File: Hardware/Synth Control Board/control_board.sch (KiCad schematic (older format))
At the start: 48 parts, among them J1 Conn_01x13, J10 Conn_01x05, J11 Conn_01x08, J2 Conn_01x03, J3 Conn_01x13, J4 Conn_01x13, J5 Conn_01x08, J6 Conn_01x13, J7 Conn_01x05, J8 Conn_01x05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

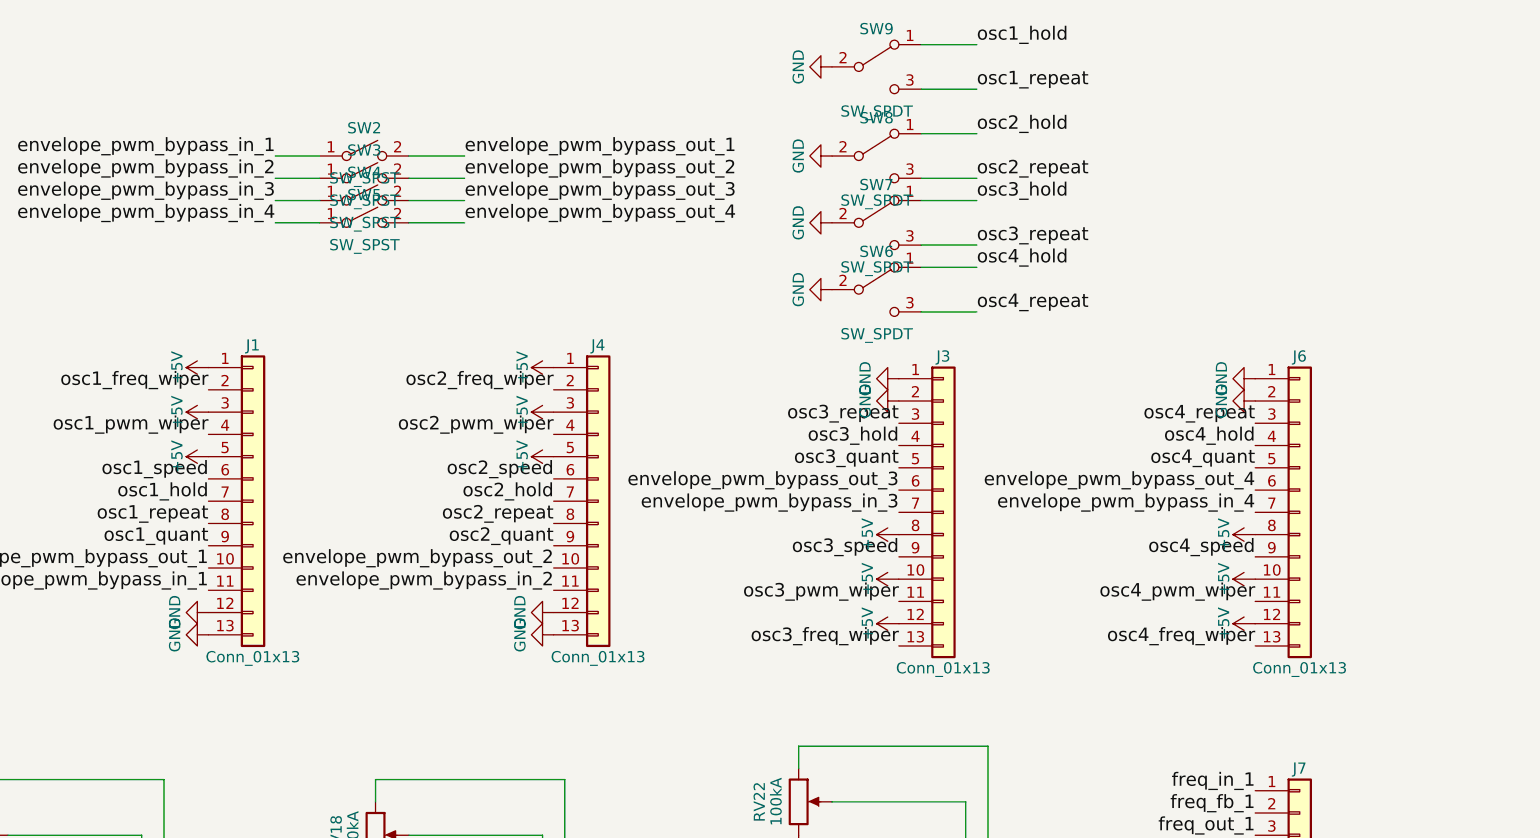
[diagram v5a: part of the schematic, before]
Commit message: add quantization again, fix connectors again, add mounting holes to main board
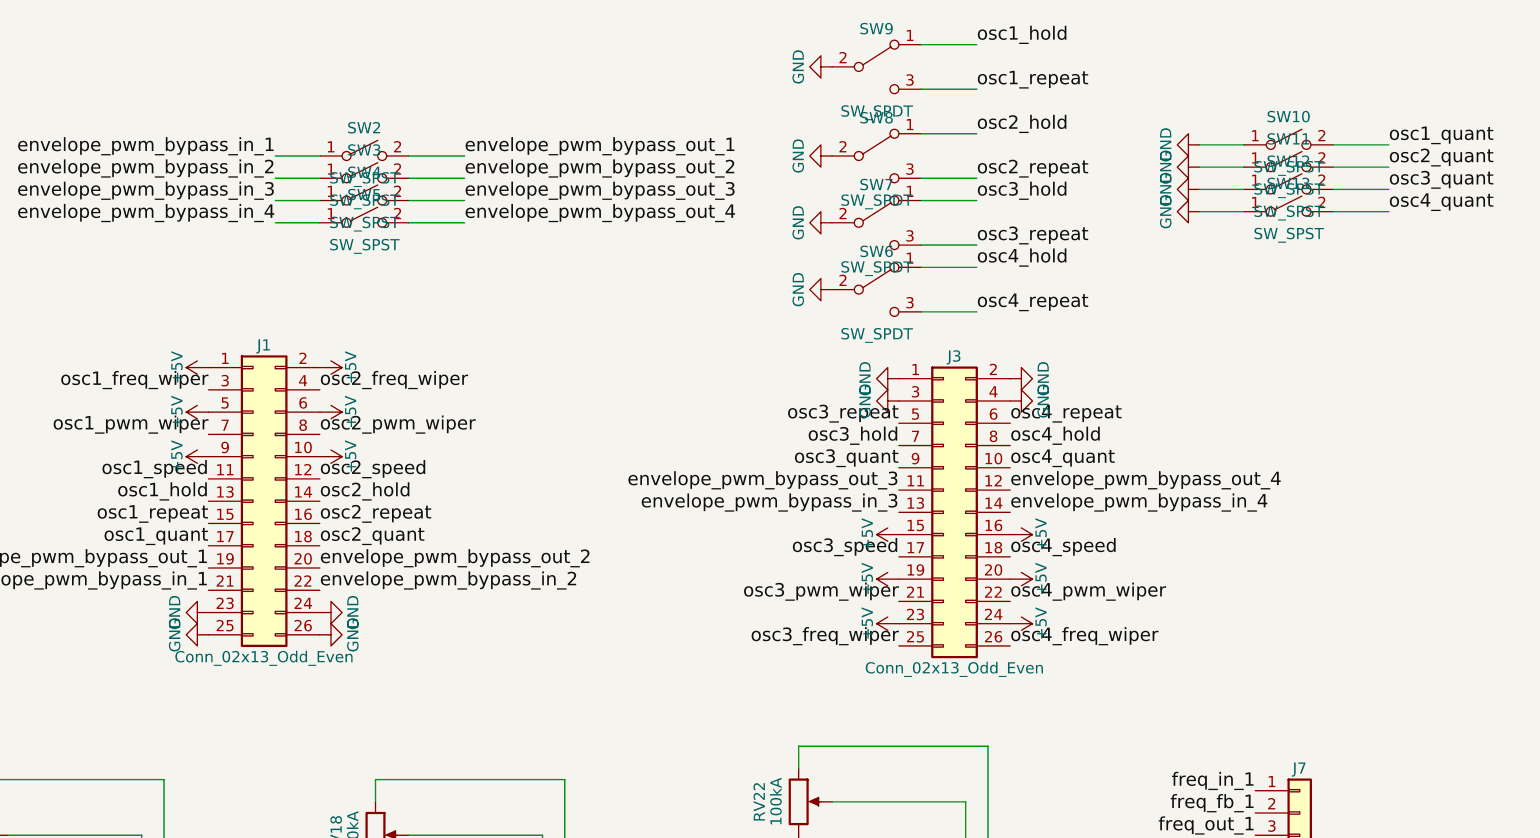
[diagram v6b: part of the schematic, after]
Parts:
- removed J1, J3, J4, J6: Conn_01x13, Pin_Headers:Pin_Header_Straight_1x13_Pitch2.54mm, symbol Conn_01x13
- added J1, J3: Conn_02x13_Odd_Even, Pin_Headers:Pin_Header_Straight_2x13_Pitch2.54mm, symbol Conn_02x13_Odd_Even
- added SW10, SW11, SW12, SW13: SW_SPST, SparkFun-Electromechanical:SWITCH-SPDT, symbol SW_SPST
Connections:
- net +5V: now also J1.1 (Pin_1), J1.10 (Pin_10), J1.2 (Pin_2), J1.5 (Pin_5), J1.6 (Pin_6), J1.9 (Pin_9), J3.15 (Pin_15), J3.16 (Pin_16), J3.19 (Pin_19), J3.20 (Pin_20), J3.23 (Pin_23), J3.24 (Pin_24)
- net GND: now also J1.23 (Pin_23), J1.24 (Pin_24), J1.25 (Pin_25), J1.26 (Pin_26), J3.1 (Pin_1), J3.2 (Pin_2), J3.3 (Pin_3), J3.4 (Pin_4), SW10.1 (A), SW11.1 (A), SW12.1 (A), SW13.1 (A)
- net envelope_pwm_bypass_in_1: now also J1.21 (Pin_21)
- net envelope_pwm_bypass_in_2: now also J1.22 (Pin_22)
- net envelope_pwm_bypass_in_3: now also J3.13 (Pin_13)
- net envelope_pwm_bypass_in_4: now also J3.14 (Pin_14)
- net envelope_pwm_bypass_out_1: now also J1.19 (Pin_19)
- net envelope_pwm_bypass_out_2: now also J1.20 (Pin_20)
- net envelope_pwm_bypass_out_3: now also J3.11 (Pin_11)
- net envelope_pwm_bypass_out_4: now also J3.12 (Pin_12)
- net osc1_freq_wiper: now also J1.3 (Pin_3)
- net osc1_hold: now also J1.13 (Pin_13)
- net osc1_pwm_wiper: now also J1.7 (Pin_7)
- net osc1_quant: now also J1.17 (Pin_17), SW10.2 (B)
- net osc1_repeat: now also J1.15 (Pin_15)
- net osc1_speed: now also J1.11 (Pin_11)
- net osc2_freq_wiper: now also J1.4 (Pin_4)
- net osc2_hold: now also J1.14 (Pin_14)
- net osc2_pwm_wiper: now also J1.8 (Pin_8)
- net osc2_quant: now also J1.18 (Pin_18), SW11.2 (B)
- net osc2_repeat: now also J1.16 (Pin_16)
- net osc2_speed: now also J1.12 (Pin_12)
- net osc3_freq_wiper: now also J3.25 (Pin_25)
- net osc3_hold: now also J3.7 (Pin_7)
- net osc3_pwm_wiper: now also J3.21 (Pin_21)
- net osc3_quant: now also J3.9 (Pin_9), SW12.2 (B)
- net osc3_repeat: now also J3.5 (Pin_5)
- net osc3_speed: now also J3.17 (Pin_17)
- net osc4_freq_wiper: now also J3.26 (Pin_26)
- net osc4_hold: now also J3.8 (Pin_8)
- net osc4_pwm_wiper: now also J3.22 (Pin_22)
- net osc4_quant: now also J3.10 (Pin_10), SW13.2 (B)
- net osc4_repeat: now also J3.6 (Pin_6)
- net osc4_speed: now also J3.18 (Pin_18)

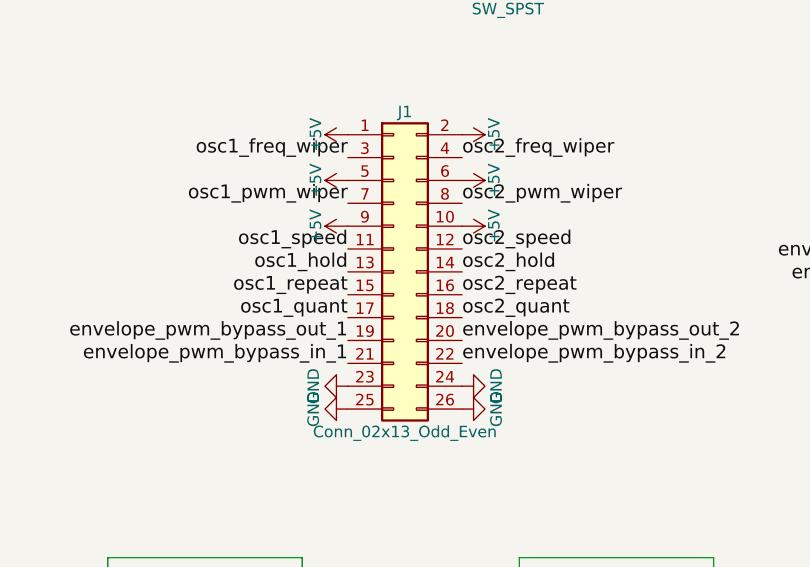
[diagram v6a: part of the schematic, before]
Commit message: reroute first connector on main board
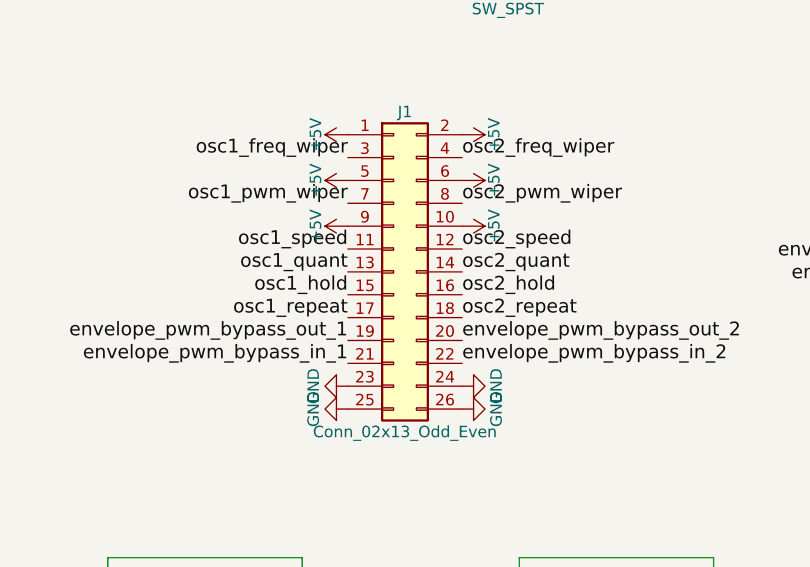
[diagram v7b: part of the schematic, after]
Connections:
- net osc1_hold: now also J1.15 (Pin_15); no longer J1.13 (Pin_13)
- net osc1_quant: now also J1.13 (Pin_13); no longer J1.17 (Pin_17)
- net osc1_repeat: now also J1.17 (Pin_17); no longer J1.15 (Pin_15)
- net osc2_hold: now also J1.16 (Pin_16); no longer J1.14 (Pin_14)
- net osc2_quant: now also J1.14 (Pin_14); no longer J1.18 (Pin_18)
- net osc2_repeat: now also J1.18 (Pin_18); no longer J1.16 (Pin_16)
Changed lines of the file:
@@
 Text Label 5700 2850 2    60   ~ 0
 envelope_pwm_bypass_out_1
-Text Label 5700 2650 2    60   ~ 0
+Text Label 5700 2750 2    60   ~ 0
 osc1_repeat
-Text Label 5700 2750 2    60   ~ 0
+Text Label 5700 2550 2    60   ~ 0
 osc1_quant
 Text Label 2650 5550 2    60   ~ 0
@@
 	0    -1   -1   0
 $EndComp
-Text Label 5700 2550 2    60   ~ 0
+Text Label 5700 2650 2    60   ~ 0
 osc1_hold
 Wire Wire Line
@@
 Text Label 6200 2850 0    60   ~ 0
 envelope_pwm_bypass_out_2
-Text Label 6200 2650 0    60   ~ 0
+Text Label 6200 2750 0    60   ~ 0
 osc2_repeat
-Text Label 6200 2750 0    60   ~ 0
+Text Label 6200 2550 0    60   ~ 0
 osc2_quant
 Text Label 10400 4500 2    60   ~ 0
@@
 	0    1    -1   0
 $EndComp
-Text Label 6200 2550 0    60   ~ 0
+Text Label 6200 2650 0    60   ~ 0
 osc2_hold
 Wire Wire Line

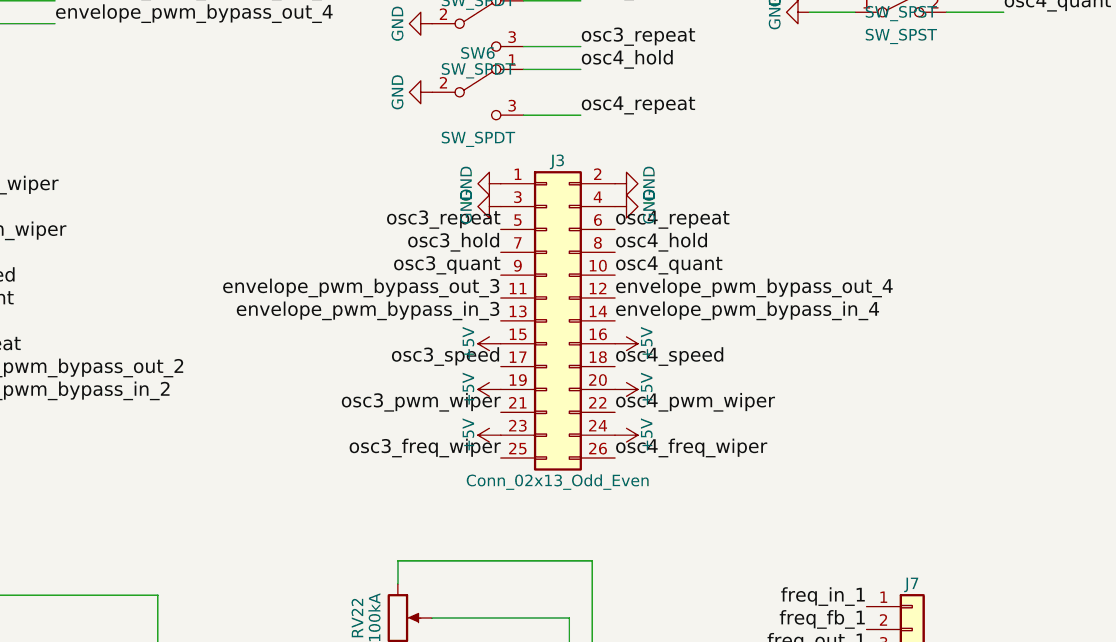
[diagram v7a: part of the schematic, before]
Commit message: reroute connector board with 2-row connectors. Hold switch placement is temporary. Need to find room for this.
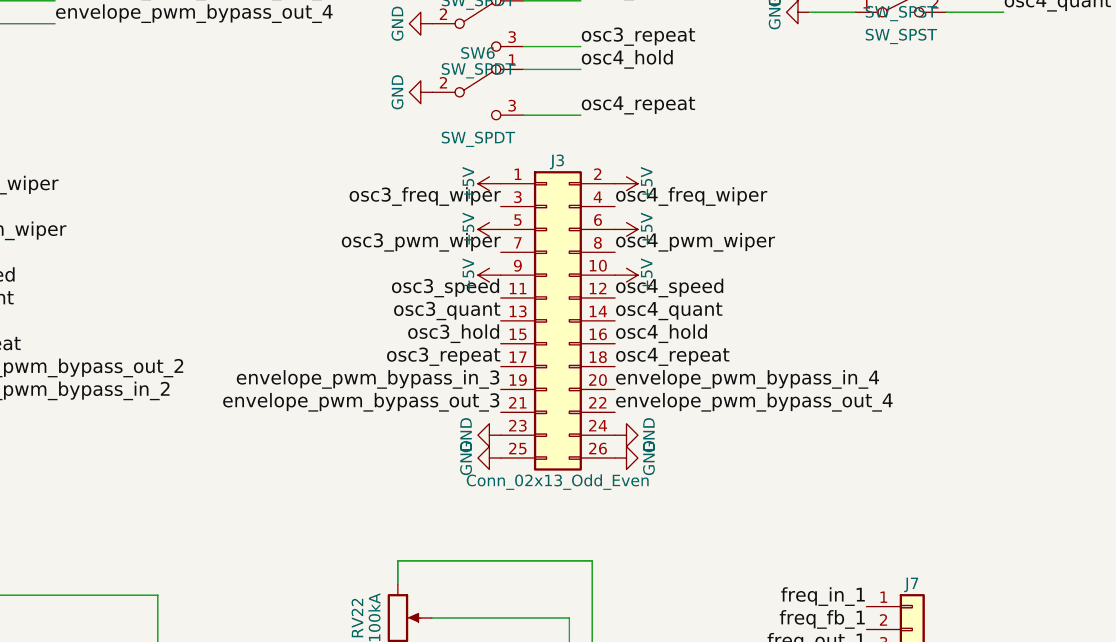
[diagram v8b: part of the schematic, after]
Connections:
- net +5V: now also J3.1 (Pin_1), J3.10 (Pin_10), J3.2 (Pin_2), J3.5 (Pin_5), J3.6 (Pin_6), J3.9 (Pin_9); no longer J3.15 (Pin_15), J3.16 (Pin_16), J3.19 (Pin_19), J3.20 (Pin_20), J3.23 (Pin_23), J3.24 (Pin_24)
- net GND: now also J3.23 (Pin_23), J3.24 (Pin_24), J3.25 (Pin_25), J3.26 (Pin_26); no longer J3.1 (Pin_1), J3.2 (Pin_2), J3.3 (Pin_3), J3.4 (Pin_4)
- net envelope_pwm_bypass_in_3: now also J3.19 (Pin_19); no longer J3.13 (Pin_13)
- net envelope_pwm_bypass_in_4: now also J3.20 (Pin_20); no longer J3.14 (Pin_14)
- net envelope_pwm_bypass_out_3: now also J3.21 (Pin_21); no longer J3.11 (Pin_11)
- net envelope_pwm_bypass_out_4: now also J3.22 (Pin_22); no longer J3.12 (Pin_12)
- net osc3_freq_wiper: now also J3.3 (Pin_3); no longer J3.25 (Pin_25)
- net osc3_hold: now also J3.15 (Pin_15); no longer J3.7 (Pin_7)
- net osc3_pwm_wiper: now also J3.7 (Pin_7); no longer J3.21 (Pin_21)
- net osc3_quant: now also J3.13 (Pin_13); no longer J3.9 (Pin_9)
- net osc3_repeat: now also J3.17 (Pin_17); no longer J3.5 (Pin_5)
- net osc3_speed: now also J3.11 (Pin_11); no longer J3.17 (Pin_17)
- net osc4_freq_wiper: now also J3.4 (Pin_4); no longer J3.26 (Pin_26)
- net osc4_hold: now also J3.16 (Pin_16); no longer J3.8 (Pin_8)
- net osc4_pwm_wiper: now also J3.8 (Pin_8); no longer J3.22 (Pin_22)
- net osc4_quant: now also J3.14 (Pin_14); no longer J3.10 (Pin_10)
- net osc4_repeat: now also J3.18 (Pin_18); no longer J3.6 (Pin_6)
- net osc4_speed: now also J3.12 (Pin_12); no longer J3.18 (Pin_18)
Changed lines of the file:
@@
 Wire Wire Line
 	6200 3150 6200 3150
-Text Label 8800 3200 2    60   ~ 0
+Text Label 8800 2100 2    60   ~ 0
 osc3_freq_wiper
+Text Label 8800 2300 2    60   ~ 0
+osc3_pwm_wiper
+Text Label 8800 2500 2    60   ~ 0
+osc3_speed
+Text Label 8800 2900 2    60   ~ 0
+envelope_pwm_bypass_in_3
 Text Label 8800 3000 2    60   ~ 0
-osc3_pwm_wiper
+envelope_pwm_bypass_out_3
 Text Label 8800 2800 2    60   ~ 0
-osc3_speed
+osc3_repeat
 Text Label 8800 2600 2    60   ~ 0
-envelope_pwm_bypass_in_3
-Text Label 8800 2500 2    60   ~ 0
-envelope_pwm_bypass_out_3
-Text Label 8800 2200 2    60   ~ 0
-osc3_repeat
-Text Label 8800 2400 2    60   ~ 0
 osc3_quant
 Text Label 10400 5200 2    60   ~ 0
@@
 L +5V #PWR037
 U 1 1 5C6257DA
-P 8800 3100
-F 0 "#PWR037" H 8800 2950 50  0001 C CNN
-F 1 "+5V" H 8800 3240 50  0000 C CNN
-F 2 "" H 8800 3100 50  0001 C CNN
-F 3 "" H 8800 3100 50  0001 C CNN
-	1    8800 3100
-	0    -1   -1   0
-$EndComp
-$Comp
-L GND #PWR038
-U 1 1 5C6257E0
 P 8800 2000
-F 0 "#PWR038" H 8800 1750 50  0001 C CNN
-F 1 "GND" H 8800 1850 50  0000 C CNN
+F 0 "#PWR037" H 8800 1850 50  0001 C CNN
+F 1 "+5V" H 8800 2140 50  0000 C CNN
 F 2 "" H 8800 2000 50  0001 C CNN
 F 3 "" H 8800 2000 50  0001 C CNN
 	1    8800 2000
-	0    1    1    0
+	0    -1   1    0
+$EndComp
+$Comp
+L GND #PWR038
+U 1 1 5C6257E0
+P 8800 3200
+F 0 "#PWR038" H 8800 2950 50  0001 C CNN
+F 1 "GND" H 8800 3050 50  0000 C CNN
+F 2 "" H 8800 3200 50  0001 C CNN
+F 3 "" H 8800 3200 50  0001 C CNN
+	1    8800 3200
+	0    1    -1   0
 $EndComp
 Text Label 10400 5300 2    60   ~ 0
@@
 L +5V #PWR039
 U 1 1 5C6257EF
-P 8800 2900
-F 0 "#PWR039" H 8800 2750 50  0001 C CNN
-F 1 "+5V" H 8800 3040 50  0000 C CNN
-F 2 "" H 8800 2900 50  0001 C CNN
-F 3 "" H 8800 2900 50  0001 C CNN
-	1    8800 2900
-	0    -1   -1   0
+P 8800 2200
+F 0 "#PWR039" H 8800 2050 50  0001 C CNN
+F 1 "+5V" H 8800 2340 50  0000 C CNN
+F 2 "" H 8800 2200 50  0001 C CNN
+F 3 "" H 8800 2200 50  0001 C CNN
+	1    8800 2200
+	0    -1   1    0
 $EndComp
 $Comp
 L +5V #PWR040
 U 1 1 5C6257F5
-P 8800 2700
-F 0 "#PWR040" H 8800 2550 50  0001 C CNN
-F 1 "+5V" H 8800 2840 50  0000 C CNN
-F 2 "" H 8800 2700 50  0001 C CNN
-F 3 "" H 8800 2700 50  0001 C CNN
-	1    8800 2700
-	0    -1   -1   0
-$EndComp
-Text Label 8800 2300 2    60   ~ 0
+P 8800 2400
+F 0 "#PWR040" H 8800 2250 50  0001 C CNN
+F 1 "+5V" H 8800 2540 50  0000 C CNN
+F 2 "" H 8800 2400 50  0001 C CNN
+F 3 "" H 8800 2400 50  0001 C CNN
+	1    8800 2400
+	0    -1   1    0
+$EndComp
+Text Label 8800 2700 2    60   ~ 0
 osc3_hold
-Text Label 9300 3200 0    60   ~ 0
+Text Label 9300 2100 0    60   ~ 0
 osc4_freq_wiper
+Text Label 9300 2300 0    60   ~ 0
+osc4_pwm_wiper
+Text Label 9300 2500 0    60   ~ 0
+osc4_speed
+Text Label 9300 2900 0    60   ~ 0
+envelope_pwm_bypass_in_4
 Text Label 9300 3000 0    60   ~ 0
-osc4_pwm_wiper
+envelope_pwm_bypass_out_4
 Text Label 9300 2800 0    60   ~ 0
-osc4_speed
+osc4_repeat
 Text Label 9300 2600 0    60   ~ 0
-envelope_pwm_bypass_in_4
-Text Label 9300 2500 0    60   ~ 0
-envelope_pwm_bypass_out_4
-Text Label 9300 2200 0    60   ~ 0
-osc4_repeat
-Text Label 9300 2400 0    60   ~ 0
 osc4_quant
 Text Label 10400 5900 2    60   ~ 0
@@
 L +5V #PWR041
 U 1 1 5C62580C
-P 9300 3100
-F 0 "#PWR041" H 9300 2950 50  0001 C CNN
-F 1 "+5V" H 9300 3240 50  0000 C CNN
-F 2 "" H 9300 3100 50  0001 C CNN
-F 3 "" H 9300 3100 50  0001 C CNN
-	1    9300 3100
-	0    1    -1   0
-$EndComp
-$Comp
-L GND #PWR042
-U 1 1 5C625812
 P 9300 2000
-F 0 "#PWR042" H 9300 1750 50  0001 C CNN
-F 1 "GND" H 9300 1850 50  0000 C CNN
+F 0 "#PWR041" H 9300 1850 50  0001 C CNN
+F 1 "+5V" H 9300 2140 50  0000 C CNN
 F 2 "" H 9300 2000 50  0001 C CNN
 F 3 "" H 9300 2000 50  0001 C CNN
 	1    9300 2000
-	0    -1   1    0
+	0    1    1    0
+$EndComp
+$Comp
+L GND #PWR042
+U 1 1 5C625812
+P 9300 3200
+F 0 "#PWR042" H 9300 2950 50  0001 C CNN
+F 1 "GND" H 9300 3050 50  0000 C CNN
+F 2 "" H 9300 3200 50  0001 C CNN
+F 3 "" H 9300 3200 50  0001 C CNN
+	1    9300 3200
+	0    -1   -1   0
 $EndComp
 Text Label 10400 6000 2    60   ~ 0
@@
 L +5V #PWR043
 U 1 1 5C625821
-P 9300 2900
-F 0 "#PWR043" H 9300 2750 50  0001 C CNN
-F 1 "+5V" H 9300 3040 50  0000 C CNN
-F 2 "" H 9300 2900 50  0001 C CNN
-F 3 "" H 9300 2900 50  0001 C CNN
-	1    9300 2900
-	0    1    -1   0
+P 9300 2200
+F 0 "#PWR043" H 9300 2050 50  0001 C CNN
+F 1 "+5V" H 9300 2340 50  0000 C CNN
+F 2 "" H 9300 2200 50  0001 C CNN
+F 3 "" H 9300 2200 50  0001 C CNN
+	1    9300 2200
+	0    1    1    0
 $EndComp
 $Comp
 L +5V #PWR044
 U 1 1 5C625827
-P 9300 2700
-F 0 "#PWR044" H 9300 2550 50  0001 C CNN
-F 1 "+5V" H 9300 2840 50  0000 C CNN
-F 2 "" H 9300 2700 50  0001 C CNN
-F 3 "" H 9300 2700 50  0001 C CNN
-	1    9300 2700
-	0    1    -1   0
-$EndComp
-Text Label 9300 2300 0    60   ~ 0
+P 9300 2400
+F 0 "#PWR044" H 9300 2250 50  0001 C CNN
+F 1 "+5V" H 9300 2540 50  0000 C CNN
+F 2 "" H 9300 2400 50  0001 C CNN
+F 3 "" H 9300 2400 50  0001 C CNN
+	1    9300 2400
+	0    1    1    0
+$EndComp
+Text Label 9300 2700 0    60   ~ 0
 osc4_hold
 $Comp
@@
 	9150 1500 8900 1500
 Wire Wire Line
-	9300 2000 9300 2000
+	9300 3200 9300 3200
 $Comp
 L SW_SPDT SW9
@@
 L GND #PWR049
 U 1 1 5C63783E
-P 8800 2100
-F 0 "#PWR049" H 8800 1850 50  0001 C CNN
-F 1 "GND" H 8800 1950 50  0000 C CNN
-F 2 "" H 8800 2100 50  0001 C CNN
-F 3 "" H 8800 2100 50  0001 C CNN
-	1    8800 2100
-	0    1    1    0
+P 8800 3100
+F 0 "#PWR049" H 8800 2850 50  0001 C CNN
+F 1 "GND" H 8800 2950 50  0000 C CNN
+F 2 "" H 8800 3100 50  0001 C CNN
+F 3 "" H 8800 3100 50  0001 C CNN
+	1    8800 3100
+	0    1    -1   0
 $EndComp
 $Comp
 L GND #PWR050
 U 1 1 5C6379D8
-P 9300 2100
-F 0 "#PWR050" H 9300 1850 50  0001 C CNN
-F 1 "GND" H 9300 1950 50  0000 C CNN
-F 2 "" H 9300 2100 50  0001 C CNN
-F 3 "" H 9300 2100 50  0001 C CNN
-	1    9300 2100
-	0    -1   1    0
-$EndComp
-$Comp
+P 9300 3100
+F 0 "#PWR050" H 9300 2850 50  0001 C CNN
+F 1 "GND" H 9300 2950 50  0000 C CNN
+F 2 "" H 9300 3100 50  0001 C CNN
+F 3 "" H 9300 3100 50  0001 C CNN
+	1    9300 3100
+	0    -1   -1   0
+$EndComp
+$Comp
